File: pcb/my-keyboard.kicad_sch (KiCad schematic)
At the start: 8 parts, among them J1 Conn_01x04_Socket, SW1 SW_Push, SW2 SW_Push, SW3 SW_Push, SW4 SW_Push, SW5 RotaryEncoder_Switch, SW6 RotaryEncoder_Switch, U1 MOUDLE-SEEEDUINO-XIAO

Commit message: New PCB and gerber files
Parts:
- added H1, H2, H3: MountingHole, MountingHole:MountingHole_3.5mm, symbol Mechanical:MountingHole
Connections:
- no-connect marks 0 -> 6

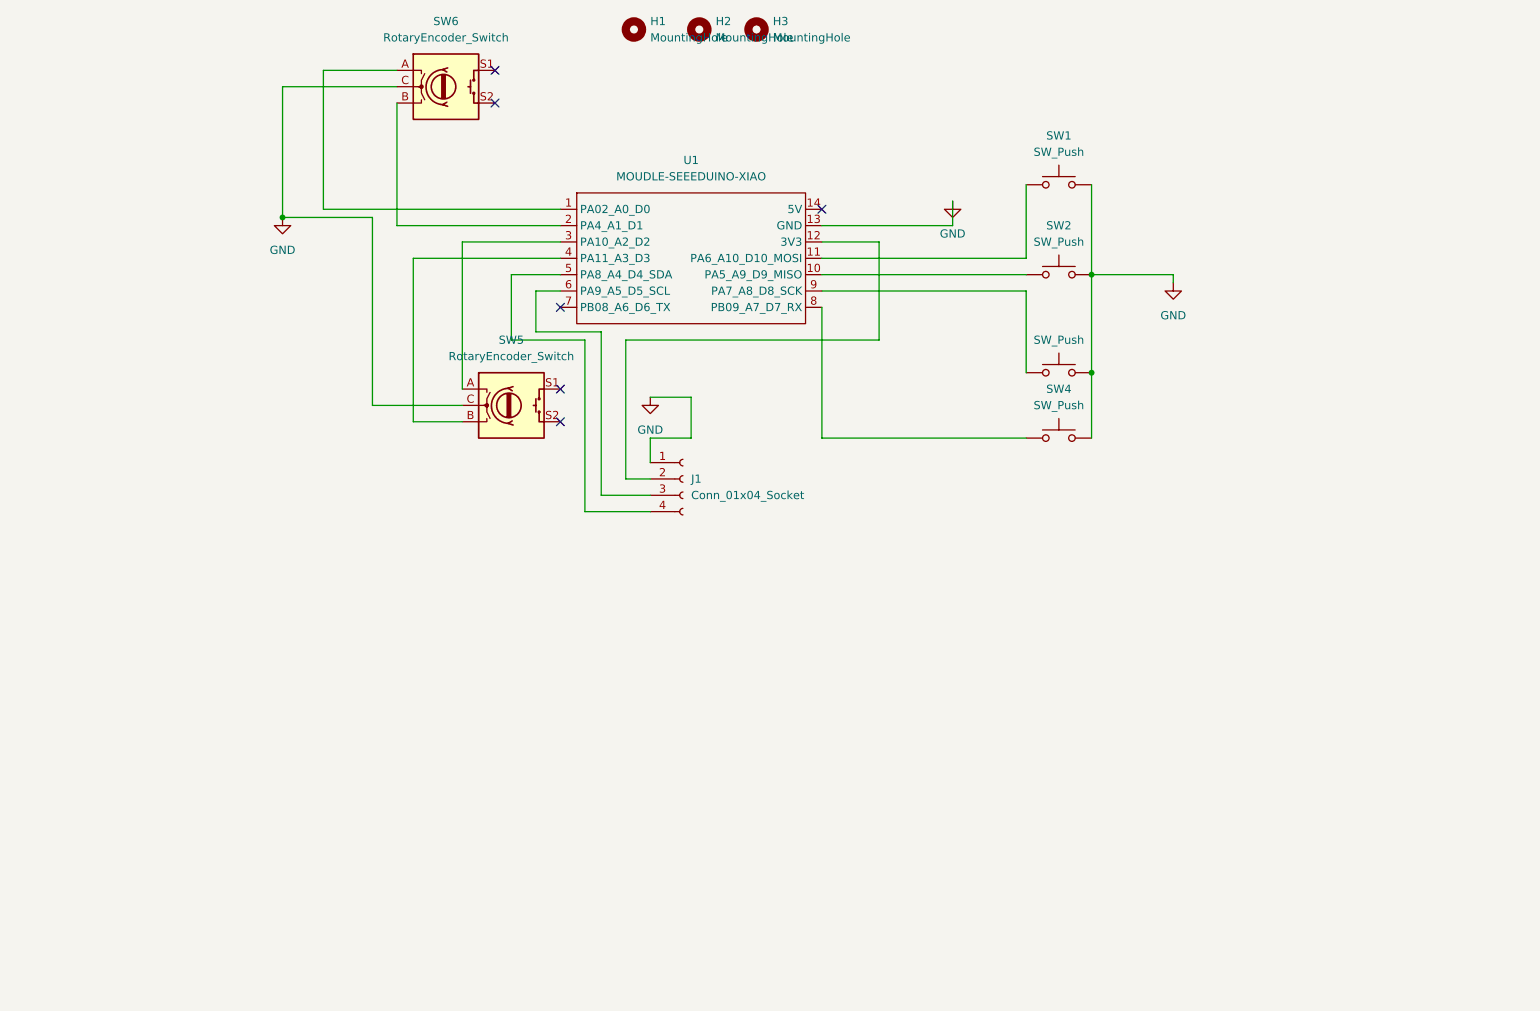
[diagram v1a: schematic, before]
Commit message: Add diodes for keyboard matrix
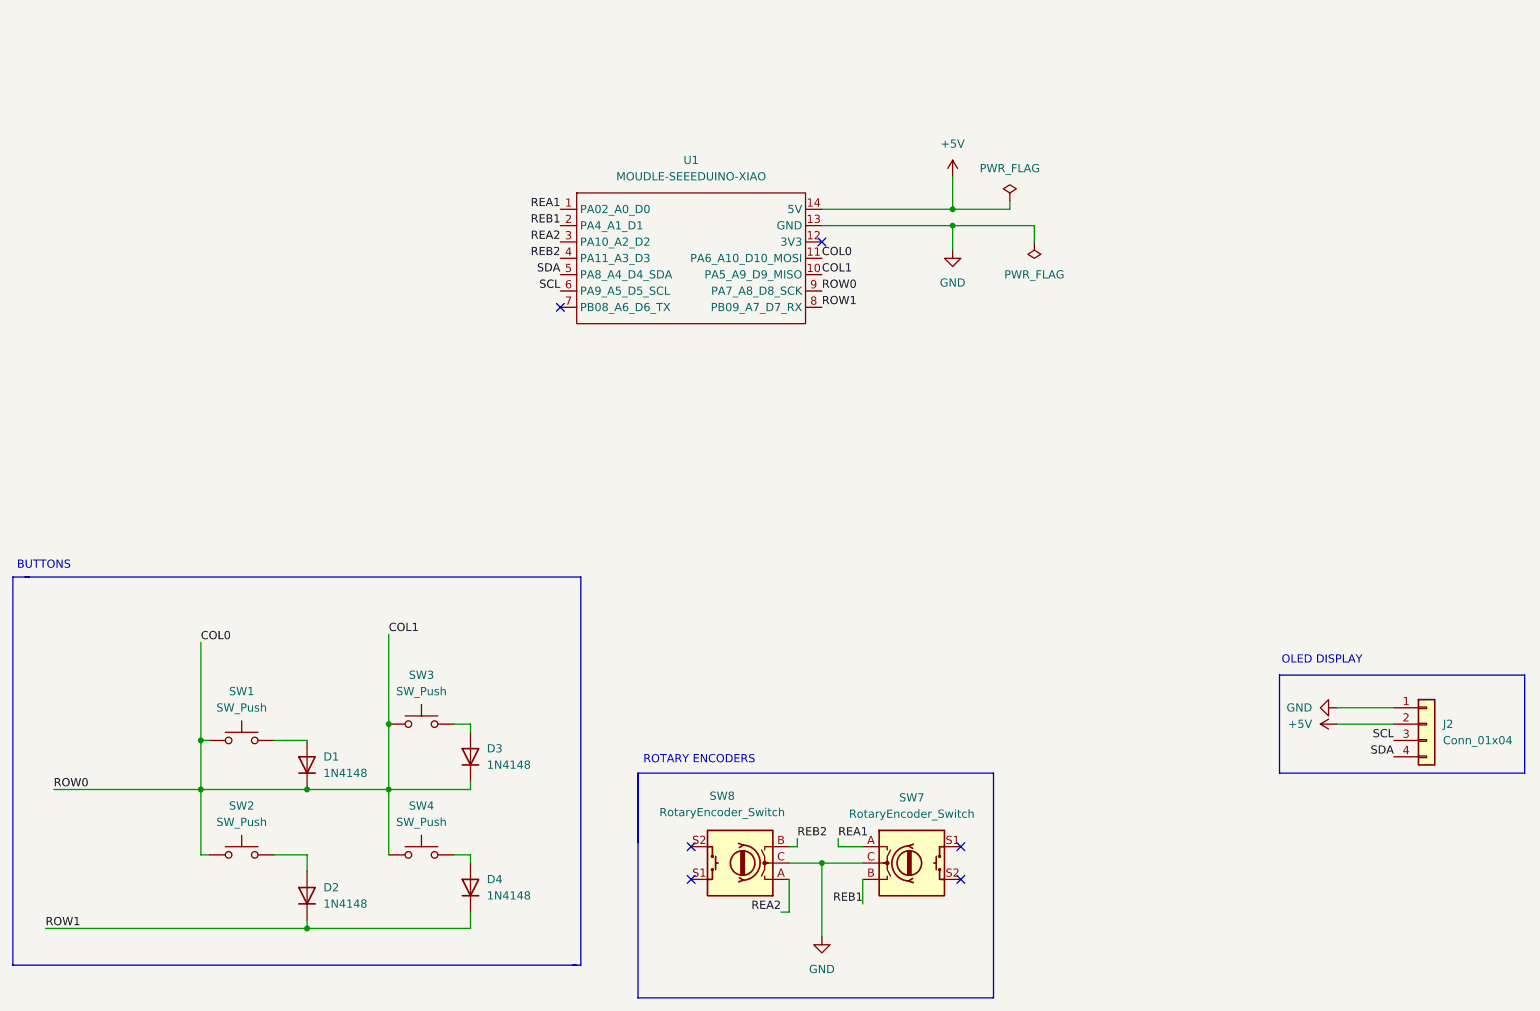
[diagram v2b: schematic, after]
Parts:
- removed H1, H2, H3: MountingHole, MountingHole:MountingHole_3.5mm, symbol Mechanical:MountingHole
- removed J1: Conn_01x04_Socket, footprints:SSD1306-0.91-OLED-4pin-128x32, symbol Connector:Conn_01x04_Socket
- removed SW5, SW6: RotaryEncoder_Switch, Rotary_Encoder:RotaryEncoder_Alps_EC11E-Switch_Vertical_H20mm, symbol Device:RotaryEncoder_Switch
- added D1, D2, D3, D4: 1N4148, Diode_THT:D_DO-35_SOD27_P7.62mm_Horizontal, symbol Diode:1N4148
- added J2: Conn_01x04, footprints:SSD1306-0.91-OLED-4pin-128x32, symbol Connector_Generic:Conn_01x04
- added SW7, SW8: RotaryEncoder_Switch, Rotary_Encoder:RotaryEncoder_Alps_EC11E-Switch_Vertical_H20mm, symbol Device:RotaryEncoder_Switch
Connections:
- net GND: now also J2.1 (Pin_1), SW7.C, SW8.C; no longer SW1.2, SW2.2, SW3.2, SW4.2
- net COL0: now reaches SW3.1, U1.9 (PA7_A8_D8_SCK)
- net COL0: now also SW1.1, SW2.1, SW4.1, U1.10 (PA5_A9_D9_MISO), U1.11 (PA6_A10_D10_MOSI), D1.1 (K), D3.1 (K)
- net ROW1: now reaches U1.8 (PB09_A7_D7_RX)
- net ROW1: now also D2.1 (K), D4.1 (K); no longer SW4.1
- net SCL: now reaches U1.6 (PA9_A5_D5_SCL)
- net SCL: now also J2.3 (Pin_3)
- net SDA: now reaches U1.5 (PA8_A4_D4_SDA)
- net SDA: now also J2.4 (Pin_4)
- net REA1: now reaches U1.1 (PA02_A0_D0)
- net REA1: now also SW7.A
- net REB1: now reaches U1.2 (PA4_A1_D1)
- net REB1: now also SW7.B
- net REA2: now reaches U1.3 (PA10_A2_D2)
- net REA2: now also SW8.A
- net REB2: now reaches U1.4 (PA11_A3_D3)
- net REB2: now also SW8.B
- net +5V: now reaches U1.14 (5V)
- net +5V: now also J2.2 (Pin_2)
- new net: D1.2 (A), SW1.2
- new net: D2.2 (A), SW2.2
- new net: D4.2 (A), SW4.2
- new net: D3.2 (A), SW3.2
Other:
- note added: "BUTTONS"
- note added: "OLED DISPLAY"
- note added: "ROTARY ENCODERS"
